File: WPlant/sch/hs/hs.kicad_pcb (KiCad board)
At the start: 2 copper layers, 5 parts, among them J1 Conn_01x03_Pin, U1 SN74LVC1G14DBV

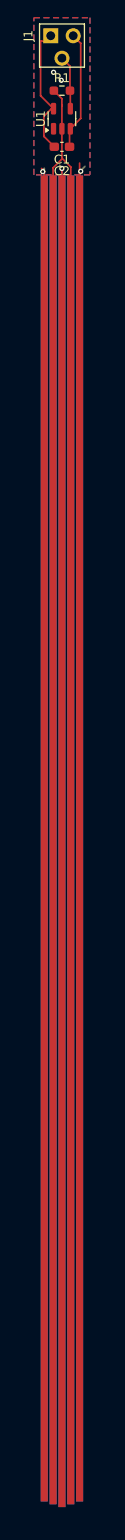
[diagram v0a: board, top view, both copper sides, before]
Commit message: Route of WP project done
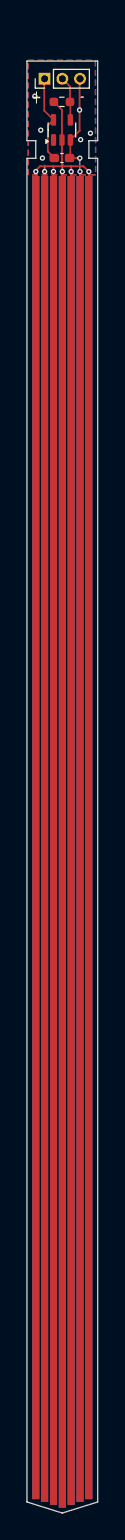
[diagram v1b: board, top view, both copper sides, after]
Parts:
- J1: footprint local:PinHeader_3 -> Connector_PinHeader_2.00mm:PinHeader_1x03_P2.00mm_Vertical
- moved J1 4.92 mm to (146.0, 28.5)
- moved C1 1.27 mm to (148.0, 37.5)
- moved R1 1.27 mm to (148.0, 31.1)
- moved U1 1.27 mm to (148.0, 34.3)
- moved C2 0.08 mm to (148.0, 39.5)
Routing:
- net Net-(C2-Pad2): track 163.1 -> 619.3 mm, vias 0 -> 4
- net /GND: track 547.0 -> 467.0 mm, vias 5 -> 10
- net Net-(J1-Pin_1): track 15.1 -> 9.99 mm
- net Net-(J1-Pin_2): track 6.10 -> 5.03 mm
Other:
- board outline added: 8 x 164.2 mm
- board text added: "+"
- board text added: "-"

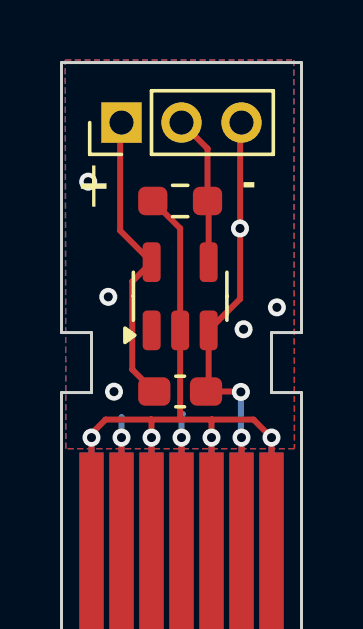
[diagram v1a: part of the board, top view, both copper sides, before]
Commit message: Update WP Sch (sheets titles, replaced wires by bus, update components values)
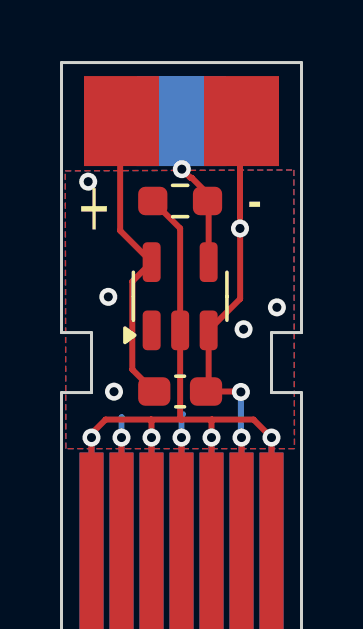
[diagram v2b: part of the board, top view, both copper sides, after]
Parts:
- J1: footprint Connector_PinHeader_2.00mm:PinHeader_1x03_P2.00mm_Vertical -> local:con3smd
- R1: value R -> 820K
- moved J1 2.00 mm to (148.0, 28.5), turned to 0 degrees
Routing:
- net Net-(J1-Pin_2): track 5.03 -> 5.10 mm, vias 0 -> 1

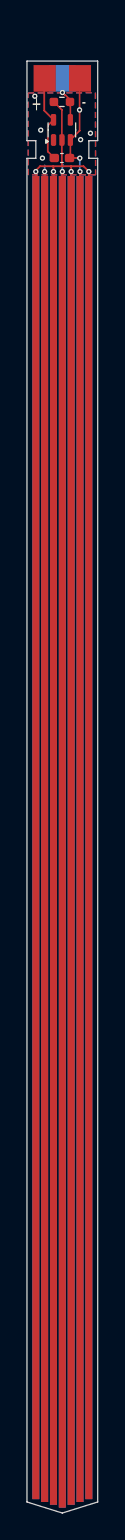
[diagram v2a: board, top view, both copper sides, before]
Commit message: Updated PCBs sent to JLPCB
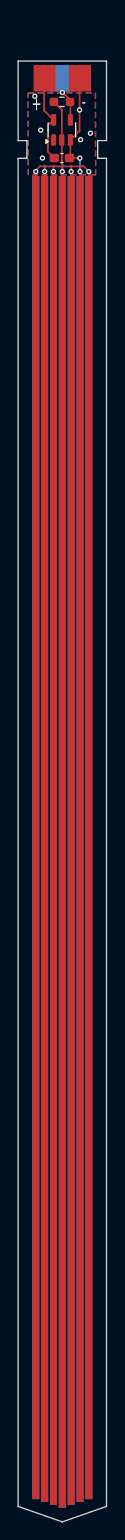
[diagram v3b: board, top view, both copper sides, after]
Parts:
- J1: value Conn_01x03_Pin -> Ext
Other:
- board size 8 x 164.2 mm -> 10 x 165.2 mm
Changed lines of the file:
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@@
+			)
+		)
+		(property "LCSC Part" "C141684"
+			(at 0 0 0)
+			(unlocked yes)
+			(layer "F.Fab")
+			(hide yes)
+			(effects
+				(font
+					(size 1.6 1)
+					(thickness 0.153)
+				)
 			)
 		)
@@
 			)
 		)
-		(property "Value" "Conn_01x03_Pin"
+		(property "Value" "Ext"
 			(at 0 1 0)
 			(unlocked yes)
@@
 			)
 		)
+		(property "LCSC Part" "C15849"
+			(at 0 0 180)
+			(unlocked yes)
+			(layer "F.Fab")
+			(hide yes)
+			(effects
+				(font
+					(size 1.6 1)
+					(thickness 0.153)
+				)
+			)
+		)
 		(property ki_fp_filters "C_*")
 		(sheetname "Root")
@@
 					(size 1.27 1.27)
 					(thickness 0.15)
+				)
+			)
+		)
+		(property "LCSC Part" "C7835"
+			(at 0 0 90)
+			(unlocked yes)
+			(layer "F.Fab")
+			(hide yes)
+			(effects
+				(font
+					(size 1.6 1)
+					(thickness 0.153)
 				)
 			)
@@
 	)
 	(gr_line
+		(start 143 35.5)
+		(end 143 26.5)
+		(stroke
+			(width 0.1)
+			(type default)
+		)
+		(layer "Edge.Cuts")
+	)
+	(gr_line
+		(start 148 191.75)
+		(end 143 190)
+		(stroke
+			(width 0.1)
+			(type default)
+		)
+		(layer "Edge.Cuts")
+	)
+	(gr_line
+		(start 152 35.5)
+		(end 152 37.5)
+		(stroke
+			(width 0.1)
+			(type default)
+		)
+		(layer "Edge.Cuts")
+	)
+	(gr_line
+		(start 143 190)
+		(end 143 37.5)
+		(stroke
+			(width 0.1)
+			(type default)
+		)
+		(layer "Edge.Cuts")
+	)
+	(gr_line
 		(start 144 35.5)
-		(end 144 26.5)
-		(stroke
-			(width 0.1)
-			(type default)
-		)
-		(layer "Edge.Cuts")
-	)
-	(gr_line
-		(start 148 190.75)
-		(end 144 189.5)
-		(stroke
-			(width 0.1)
-			(type default)
-		)
-		(layer "Edge.Cuts")
-	)
-	(gr_line
-		(start 151 35.5)
-		(end 151 37.5)
-		(stroke
-			(width 0.1)
-			(type default)
-		)
-		(layer "Edge.Cuts")
-	)
-	(gr_line
-		(start 144 189.5)
 		(end 144 37.5)
 		(stroke
@@
 	)
 	(gr_line
-		(start 145 35.5)
-		(end 145 37.5)
-		(stroke
-			(width 0.1)
-			(type default)
-		)
-		(layer "Edge.Cuts")
-	)
-	(gr_line
-		(start 152 189.5)
-		(end 148 190.75)
-		(stroke
-			(width 0.1)
-			(type default)
-		)
-		(layer "Edge.Cuts")
-	)
-	(gr_line
-		(start 152 26.5)
+		(start 153 190)
+		(end 148 191.75)
+		(stroke
+			(width 0.1)
+			(type default)
+		)
+		(layer "Edge.Cuts")
+	)
+	(gr_line
+		(start 153 26.5)
+		(end 153 35.5)
+		(stroke
+			(width 0.1)
+			(type default)
+		)
+		(layer "Edge.Cuts")
+	)
+	(gr_line
+		(start 153 35.5)
 		(end 152 35.5)
 		(stroke
@@
 	)
 	(gr_line
-		(start 152 35.5)
-		(end 151 35.5)
-		(stroke
-			(width 0.1)
-			(type default)
-		)
-		(layer "Edge.Cuts")
-	)
-	(gr_line
-		(start 145 37.5)
-		(end 144 37.5)
-		(stroke
-			(width 0.1)
-			(type default)
-		)
-		(layer "Edge.Cuts")
-	)
-	(gr_line
-		(start 144 35.5)
-		(end 145 35.5)
+		(start 144 37.5)
+		(end 143 37.5)
+		(stroke
+			(width 0.1)
+			(type default)
+		)
+		(layer "Edge.Cuts")
+	)
+	(gr_line
+		(start 143 35.5)
+		(end 144 35.5)
+		(stroke
+			(width 0.1)
+			(type default)
+		)
+		(layer "Edge.Cuts")
+	)
+	(gr_line
+		(start 153 37.5)
+		(end 153 190)
 		(stroke
 			(width 0.1)
@@
 	(gr_line
 		(start 152 37.5)
-		(end 152 189.5)
-		(stroke
-			(width 0.1)
-			(type default)
-		)
-		(layer "Edge.Cuts")
-	)
-	(gr_line
-		(start 151 37.5)
-		(end 152 37.5)
-		(stroke
-			(width 0.1)
-			(type default)
-		)
-		(layer "Edge.Cuts")
-	)
-	(gr_line
-		(start 144 26.5)
-		(end 152 26.5)
-		(stroke
-			(width 0.1)
+		(end 153 37.5)
+		(stroke
+			(width 0.1)
+			(type default)
+		)
+		(layer "Edge.Cuts")
+	)
+	(gr_line
+		(start 143 26.5)
+		(end 153 26.5)
+		(stroke
+			(width 0.1)
